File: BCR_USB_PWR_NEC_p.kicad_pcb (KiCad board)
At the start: 2 copper layers, 13.4 x 21.8 mm, 2 parts, among them CN1 DB9_Female, CN2 UE27AC54100

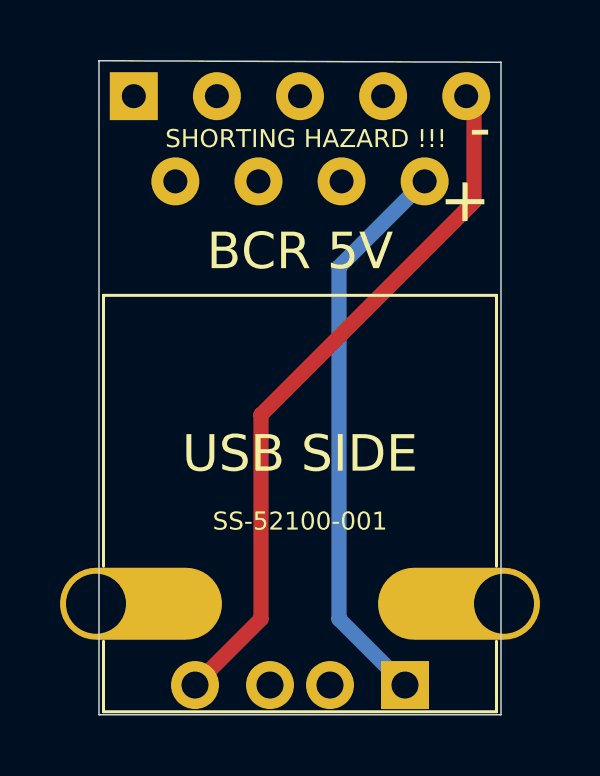
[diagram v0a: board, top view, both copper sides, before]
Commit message: shrink pcbs, 102 pcb, note short hazards
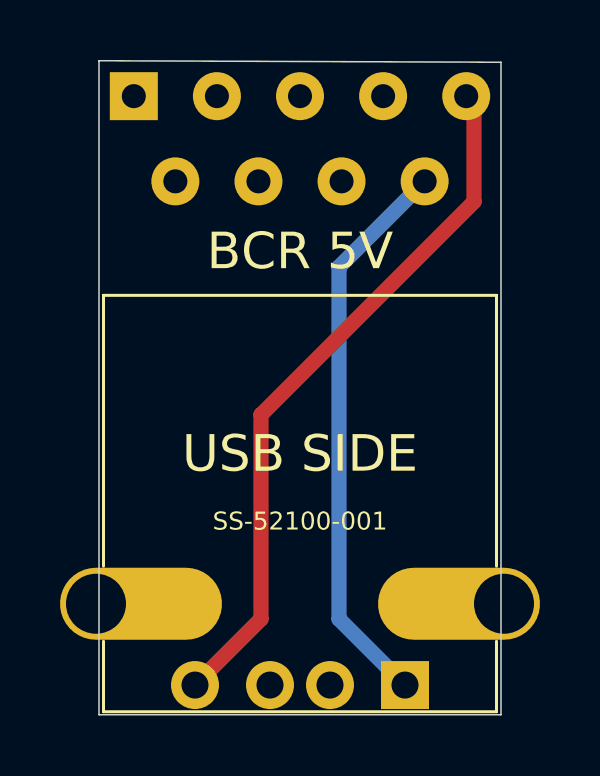
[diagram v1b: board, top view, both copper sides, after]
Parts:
- CN1: footprint 0_LOCAL:A-DF_09_PP-Z_nec -> 0_LOCAL:TE-5207826_nec
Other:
- board text removed: "+"
- board text removed: "-"
- board text removed: "SHORTING HAZARD !!!"
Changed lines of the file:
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@@
   (general
     (thickness 1.6)
-    (drawings 20)
+    (drawings 17)
     (tracks 8)
     (zones 0)
@@
     (add_net "Net-(CN2-PadSH)")
   )
-  (module 0_LOCAL:A-DF_09_PP-Z_nec (layer B.Cu)
+  (module 0_LOCAL:TE-5207826_nec (layer B.Cu)
     (at 121.46026 94.33814 180)
     (descr "9-pin D-Sub connector, straight/vertical, THT-mount, female, pitch 2.77x2.84mm, distance of mounting holes 25mm, see https://disti-assets.s3.amazonaws.com/tonar/files/datasheets/16730.pdf")
@@
     (pad 2 thru_hole circle (at -2.77 0 180) (size 1.6 1.6) (drill 0.8) (layers *.Cu *.Mask))
     (pad 1 thru_hole rect (at 0 0 180) (size 1.6 1.6) (drill 0.8) (layers *.Cu *.Mask))
-    (model ${KIPRJMOD}/3dmodels/DE9F_metal.step
-      (offset (xyz -5.54 -1.42 6.3))
+    (model ${KIPRJMOD}/3dmodels/TE-5207826_short_legs.step
+      (offset (xyz -5.528 -1.42 11.4))
       (scale (xyz 1 1 1))
       (rotate (xyz 0 0 0))
@@
     )
   )
-  (gr_text "SHORTING HAZARD !!!" (at 127.2 95.758) (layer F.SilkS)
-    (effects (font (size 0.6 0.6) (thickness 0.06)))
-  )
-  (gr_text - (at 133 95.408) (layer F.SilkS)
-    (effects (font (size 1.5 1.5) (thickness 0.15)))
-  )
-  (gr_text + (at 132.5 97.808) (layer F.SilkS)
-    (effects (font (size 1.5 1.5) (thickness 0.15)))
+  (gr_text "from BCR port" (at 126.9 104.658) (layer B.SilkS)
+    (effects (font (size 1 1) (thickness 0.1)) (justify mirror))
+  )
+  (gr_text SS-52100-001 (at 127 108.508) (layer F.SilkS)
+    (effects (font (size 0.6 0.6) (thickness 0.1)))
   )
   (gr_text "A-DF 09 PP/Z" (at 127 95.758) (layer B.SilkS)
     (effects (font (size 0.6 0.6) (thickness 0.1)) (justify mirror))
   )
-  (gr_text "from BCR port" (at 126.9 104.658) (layer B.SilkS)
-    (effects (font (size 1 1) (thickness 0.1)) (justify mirror))
-  )
-  (gr_text SS-52100-001 (at 127 108.508) (layer F.SilkS)
-    (effects (font (size 0.6 0.6) (thickness 0.1)))
-  )
   (gr_text github.com/bkw777/BCR_USB_PWR (at 127.1 109.258) (layer B.SilkS)
